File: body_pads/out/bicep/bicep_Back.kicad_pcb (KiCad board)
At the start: 2 copper layers, 228.3 x 229 mm, 0 parts

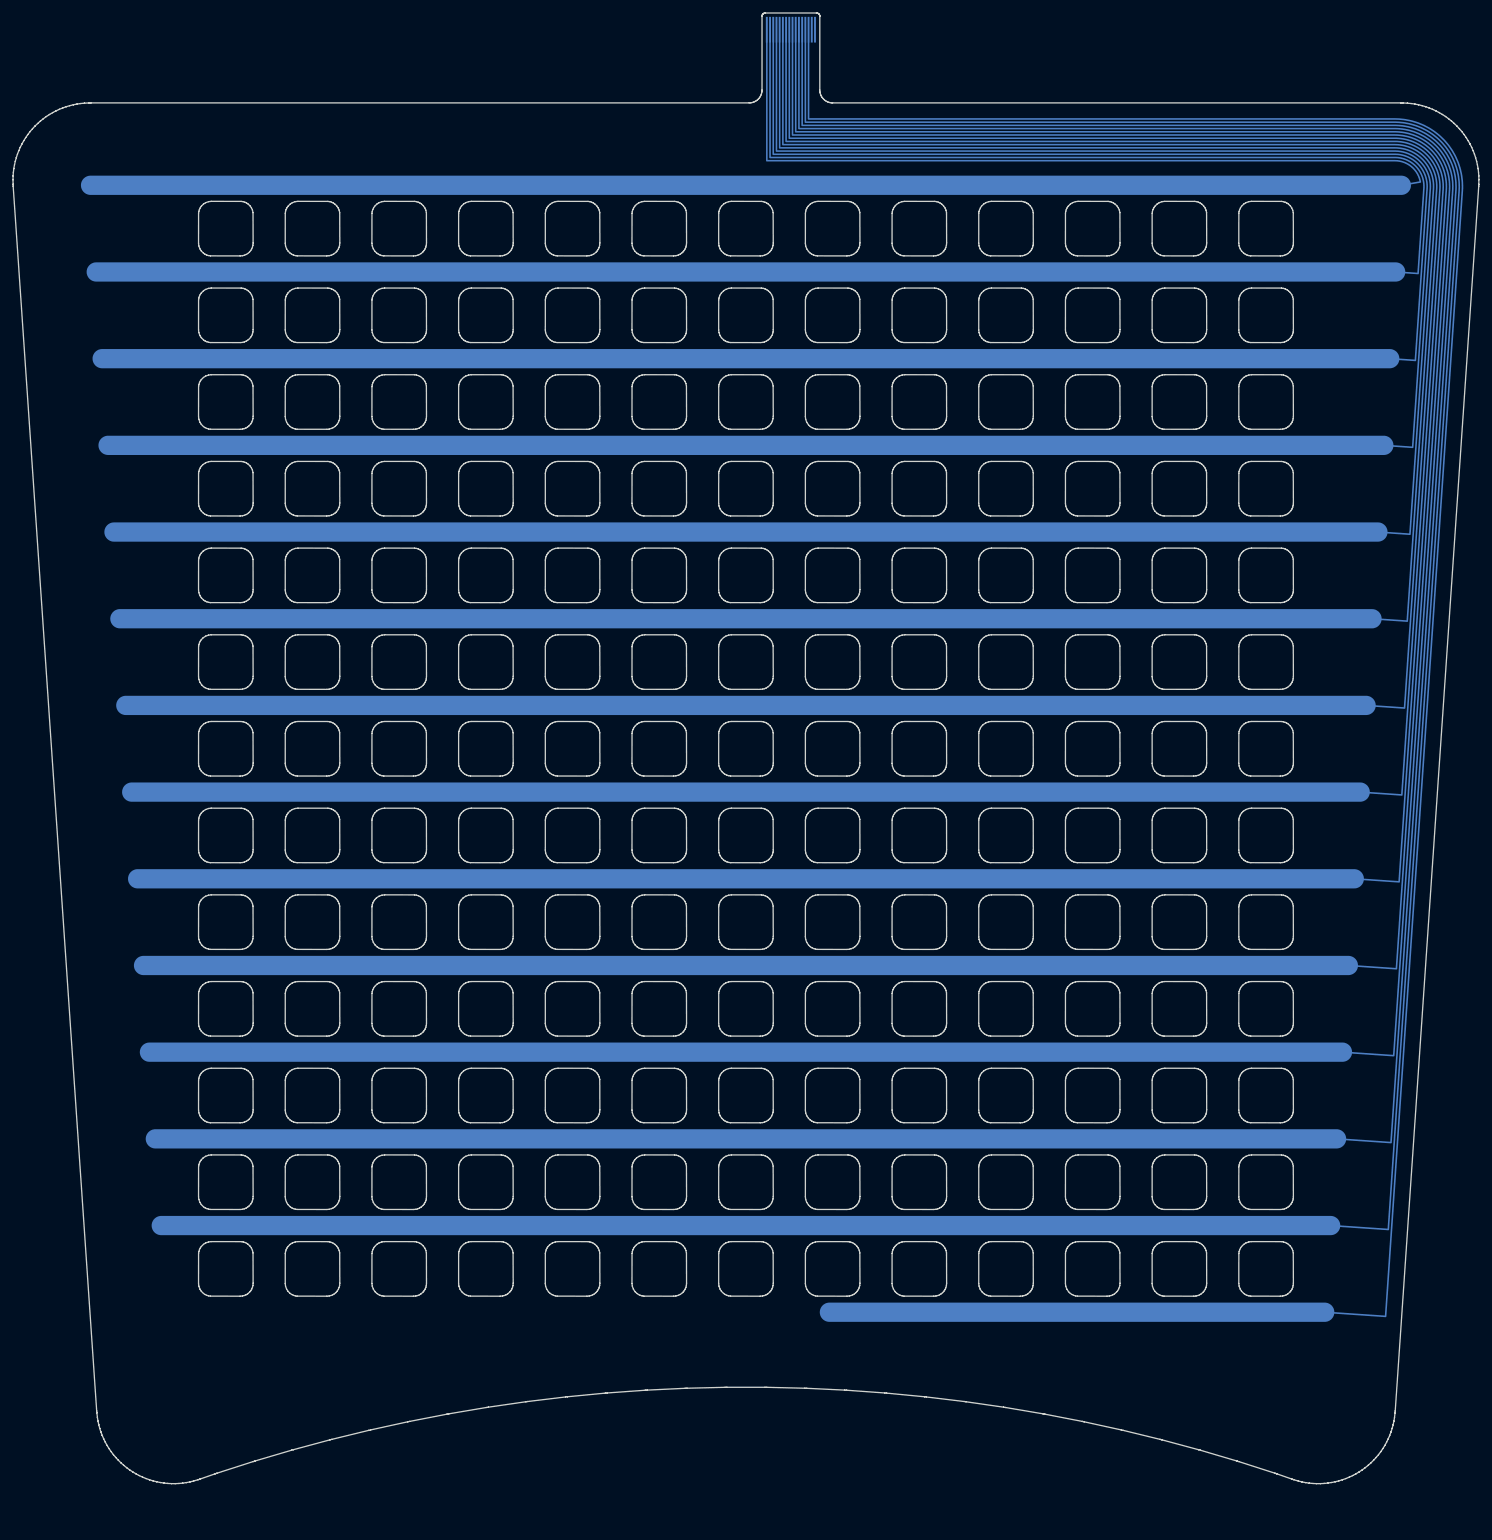
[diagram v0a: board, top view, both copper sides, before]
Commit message: Terminate body pads with vias and an FFC connector; export the full Gerber set
The pad tails now follow README Step 5 like the glove: every electrode trace
ends in a through via (0.45/0.2 mm, two staggered rows) and a 16-pin 0.5 mm
FFC connector (KiCad library Hirose FH12-16S-0.5SH) sits on the side opposite
the electrodes, making each board a 2-layer flex. A nested staircase fans the
0.5 mm bus out to the 1.0 mm via pitch and back to the 0.5 mm pads without
crossings. body_pads/kicad_post.py runs with KiCad's own python to add the
vias, footprint, connector-side tracks and nets; a .kicad_pro with flex rules
is written so kicad-cli DRC checks the right limits, and the Gerber export now
produces the same file set as the glove (both copper layers, mask, paste,
silkscreen, edge cuts, Eco1/Eco2, PTH/NPTH drills and maps).

Also: the column grid is shifted so no column exits under the tail bus, the
mirrored chest half swaps its tail order so both halves match, previews gain
a tail close-up, and the README describes the new tail, layers and checks.
Includes the body-pad documentation docx added to the working tree.

Co-Authored-By: Claude Fable 5.1 <noreply@anthropic.com>
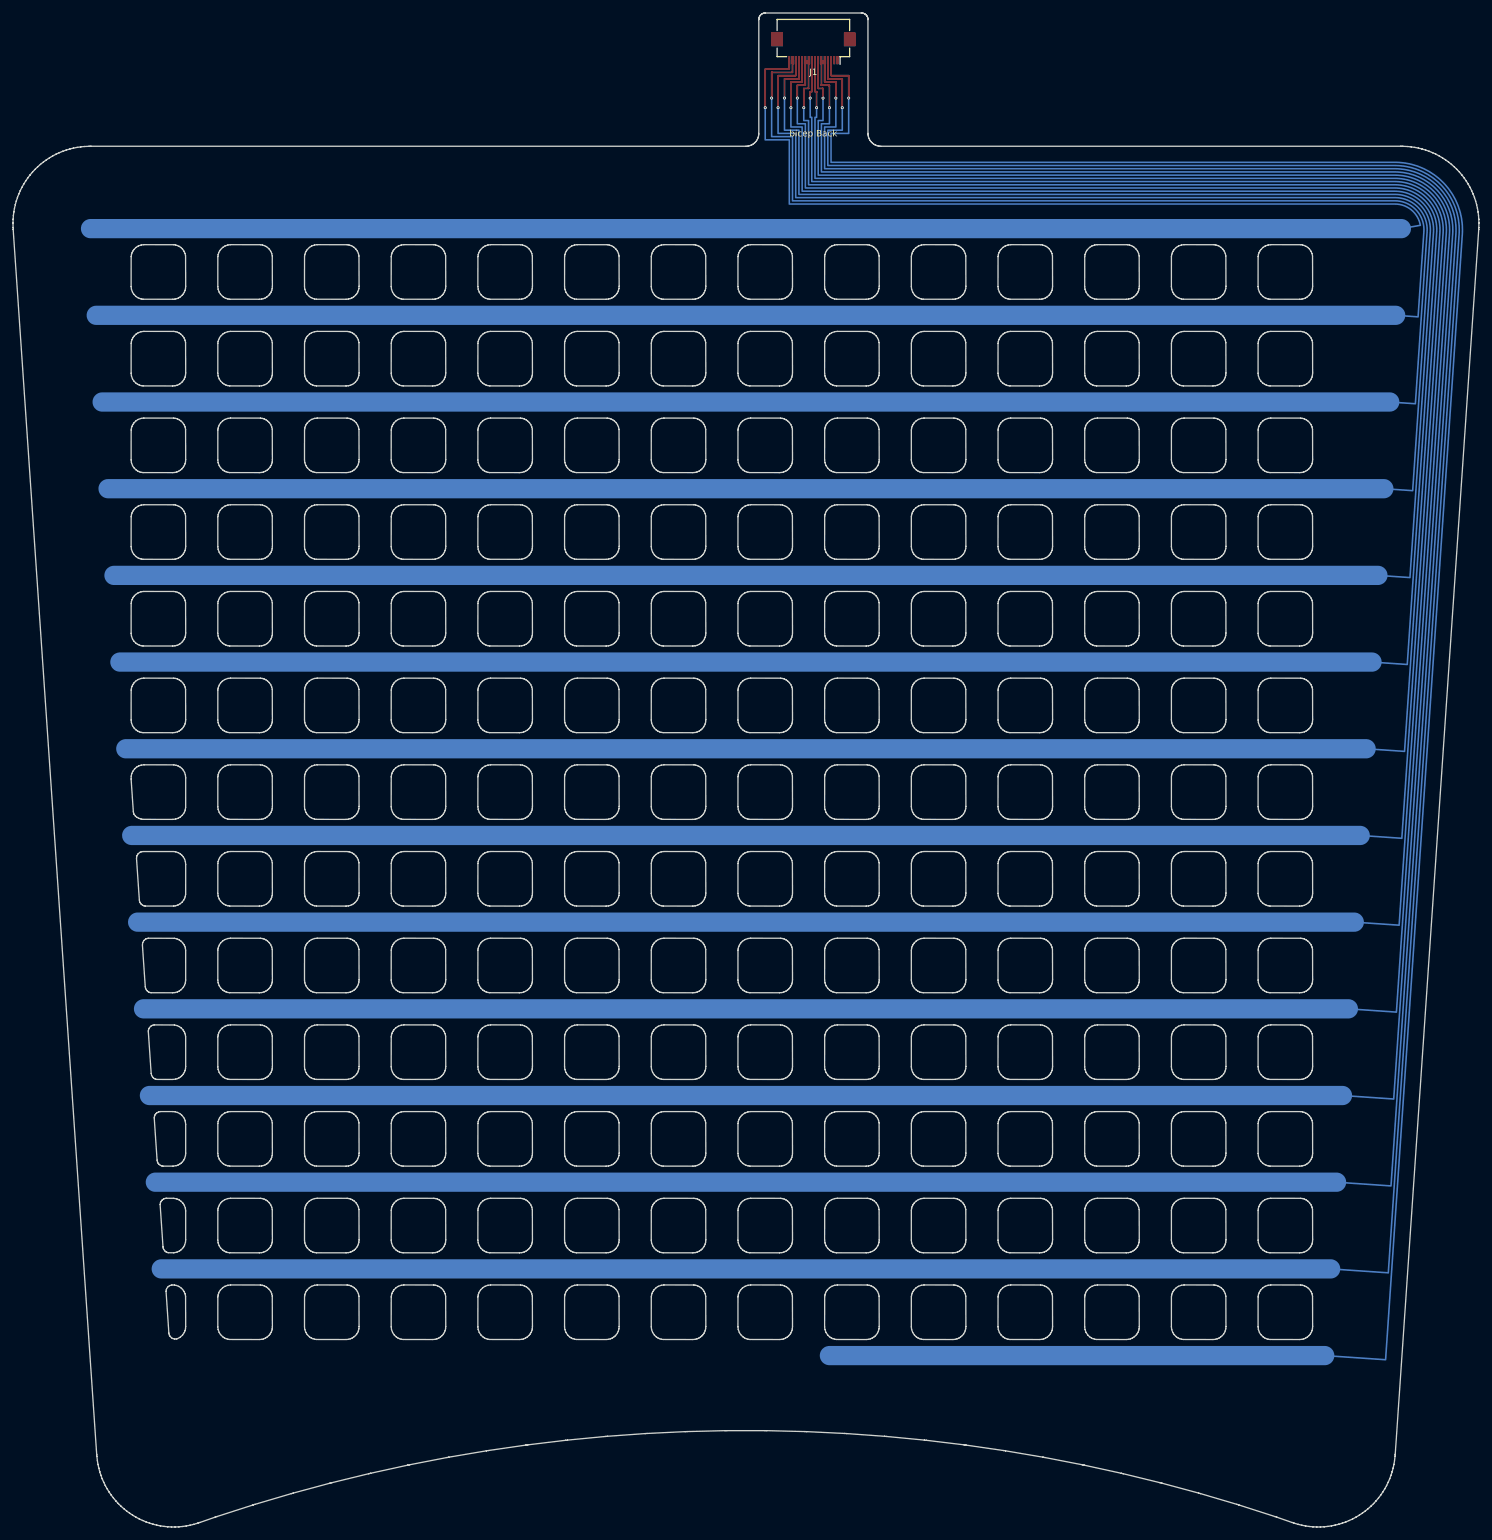
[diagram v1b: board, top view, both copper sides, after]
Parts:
- added J1: Hirose_FH12-16S-0.5SH_1x16-1MP_P0.50mm_Horizontal, Hirose_FH12-16S-0.5SH_1x16-1MP_P0.50mm_Horizontal, F.Cu at (134.6, 15.5)
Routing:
- net ROW14: track 0.00 -> 11.2 mm, vias 0 -> 1
- net ROW12: track 0.00 -> 10.2 mm, vias 0 -> 1
- net ROW02: track 0.00 -> 9.65 mm, vias 0 -> 1
- net ROW13: track 0.00 -> 9.15 mm, vias 0 -> 1
- net ROW10: track 0.00 -> 9.15 mm, vias 0 -> 1
- net ROW04: track 0.00 -> 8.65 mm, vias 0 -> 1
- net ROW01: track 0.00 -> 8.65 mm, vias 0 -> 1
- net ROW11: track 0.00 -> 8.15 mm, vias 0 -> 1
- net ROW08: track 0.00 -> 8.15 mm, vias 0 -> 1
- net ROW06: track 0.00 -> 7.65 mm, vias 0 -> 1
- net ROW03: track 0.00 -> 7.65 mm, vias 0 -> 1
- net ROW09: track 0.00 -> 7.15 mm, vias 0 -> 1
- net ROW05: track 0.00 -> 6.65 mm, vias 0 -> 1
- net ROW07: track 0.00 -> 6.15 mm, vias 0 -> 1
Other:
- board size 228.3 x 229 mm -> 228.3 x 235.8 mm
- board text added: "bicep Back"
- board text added: "bicep Back: 2-layer flex. Electrodes on B.Cu under the B.Mask opening; FFC connector J1 on F.Cu. Eco1.User = PSA adhesive on the B.Cu side. Eco2.User = stiffener under the connector (on the B.Cu side of the tail)."
- board text removed: "bicep Back: 1-layer flex, copper on B.Cu. B.Mask = coverlay openings. Eco1.User = PSA adhesive (copper side). Eco2.User = tail stiffener (opposite side), total tail 0.30 +/-0.05 mm. 16-pin 0.5 mm FFC fingers."

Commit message: Iteration 2: forearm pad from the measured paper template, bicep rescaled
The forearm outline is now digitised from the paper template wrapped round
the wearer's forearm (FOREARM_TEMPLATE_MM, scaled by the ruler in the photo):
240 mm round the arm at the elbow end, 210 mm long, narrowing to the 50 mm
underside strap at the wrist, tails on the elbow-end edge. The bicep pad is
scaled to the same arm (180 mm long, 200 -> 175 mm wide); the chest halves
are unchanged. Boards carry "iter2" in their title block and summary.json,
and all Gerbers, footprints, previews and checks are regenerated.

Also adds the template photos and the updated documentation docx.

Co-Authored-By: Claude Fable 5.1 <noreply@anthropic.com>
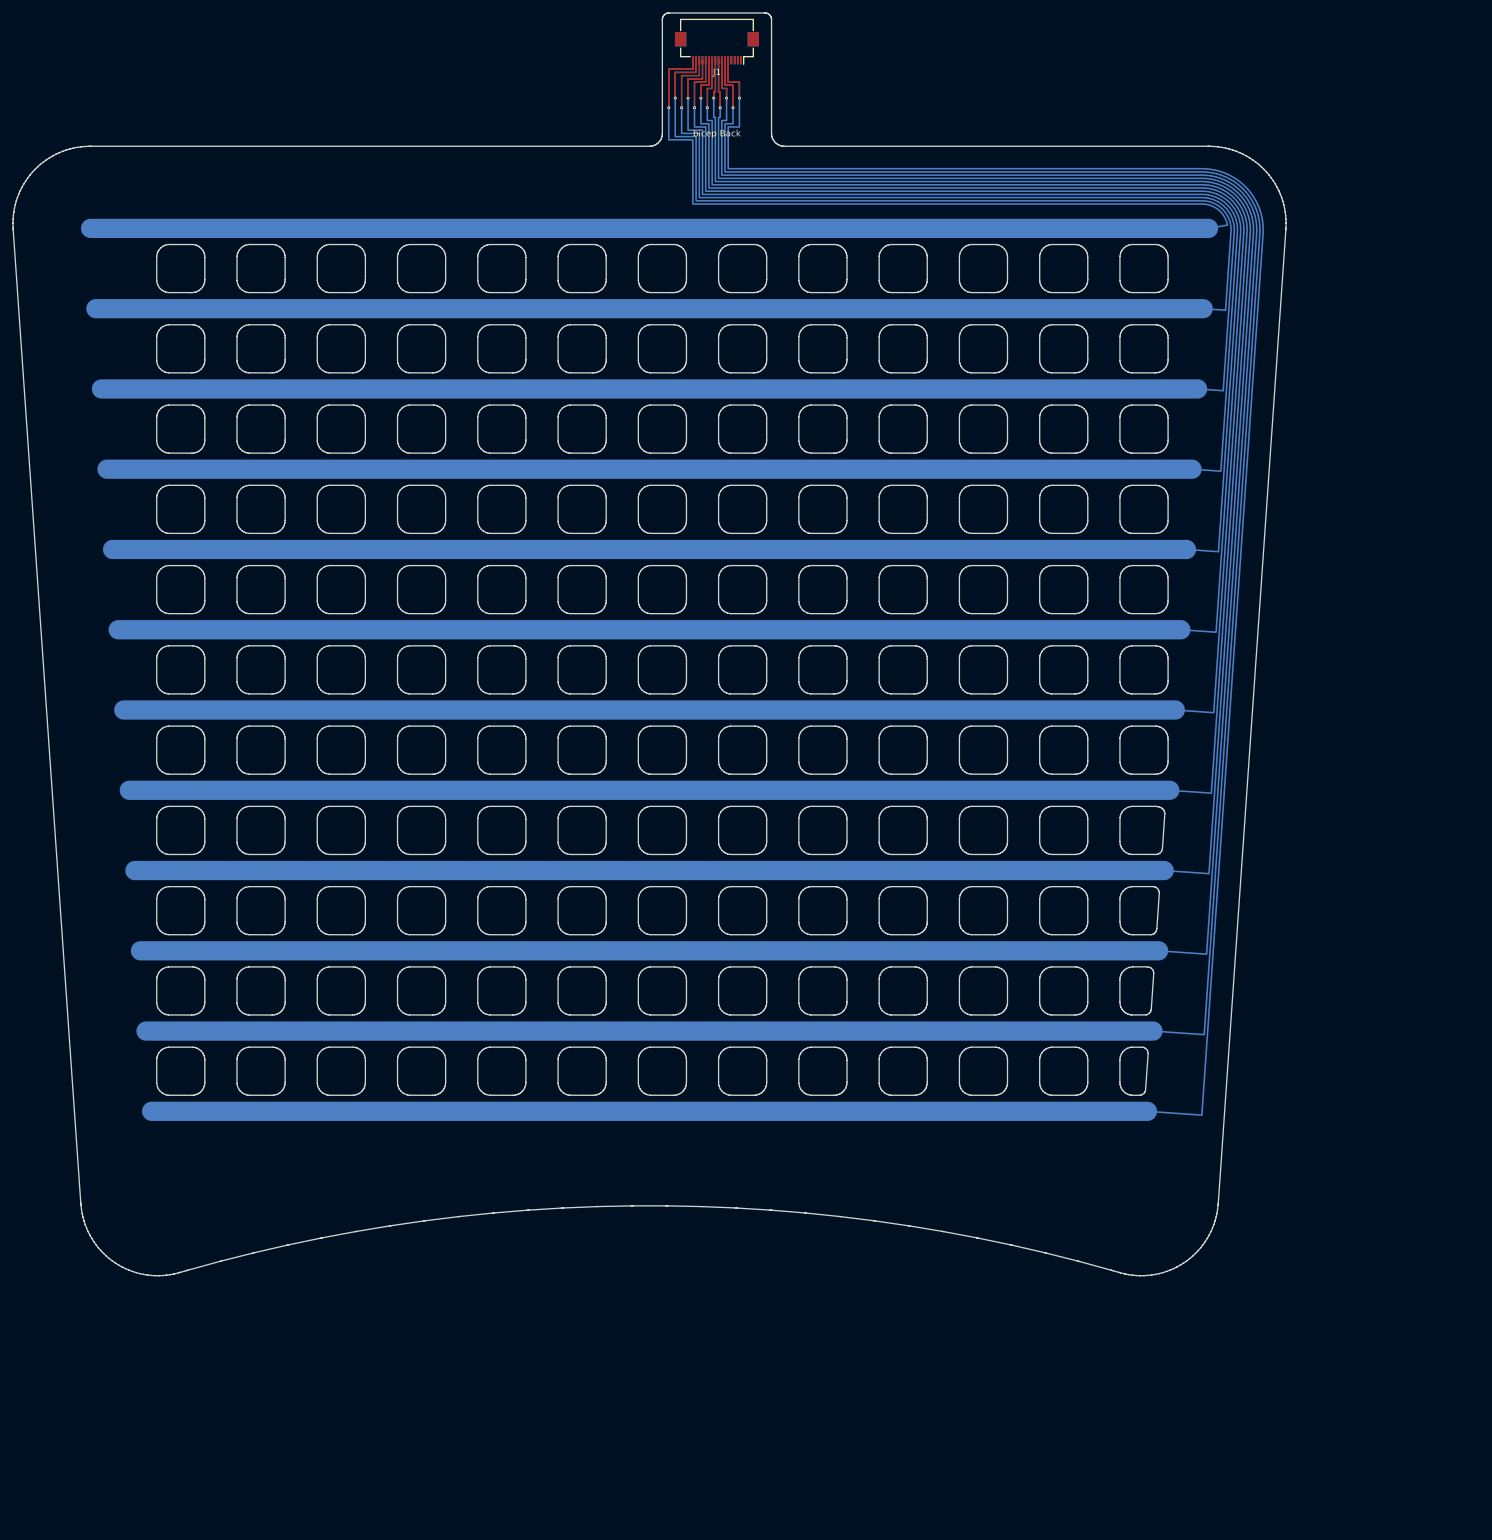
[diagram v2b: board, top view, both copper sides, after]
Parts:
- moved J1 15.0 mm to (119.6, 15.5)
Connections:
- J1 pad 10: ROW08 -> ROW06
- J1 pad 11: ROW09 -> ROW07
- J1 pad 12: ROW10 -> ROW08
- J1 pad 13: ROW11 -> ROW09
- J1 pad 14: ROW12 -> ROW10
- J1 pad 15: ROW13 -> ROW11
- J1 pad 16: ROW14 -> ROW12
- J1 pad 3: ROW01 -> (no net)
- J1 pad 4: ROW02 -> (no net)
- J1 pad 5: ROW03 -> ROW01
- J1 pad 6: ROW04 -> ROW02
- J1 pad 7: ROW05 -> ROW03
- J1 pad 8: ROW06 -> ROW04
- J1 pad 9: ROW07 -> ROW05
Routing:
- net ROW14: track 11.2 -> 0.00 mm, vias 1 -> 0
- net ROW13: track 9.15 -> 0.00 mm, vias 1 -> 0
- net ROW12: track 10.2 -> 11.2 mm
- net ROW11: track 8.15 -> 9.15 mm
- net ROW10: track 9.15 -> 10.2 mm
- net ROW09: track 7.15 -> 8.15 mm
- net ROW08: track 8.15 -> 9.15 mm
- net ROW07: track 6.15 -> 7.15 mm
- net ROW04: track 8.65 -> 7.65 mm
- net ROW03: track 7.65 -> 6.65 mm
- net ROW02: track 9.65 -> 8.65 mm
- net ROW01: track 8.65 -> 7.65 mm
- net ROW06: track 7.65 -> 8.15 mm
- net ROW05: track 6.65 -> 6.15 mm
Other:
- board size 228.3 x 235.8 mm -> 198.3 x 196.6 mm
